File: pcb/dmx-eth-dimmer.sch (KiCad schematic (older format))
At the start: 38 parts, among them J1 MAINS IN, J2 STANDARD ENC28J60, J3 MINI ENC28J60, J4 MASTER PROG, SW1 IP1, SW2 IP2, SW3 IP3, SW4 IP4, SW5 DMXAH, SW6 DMXAL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

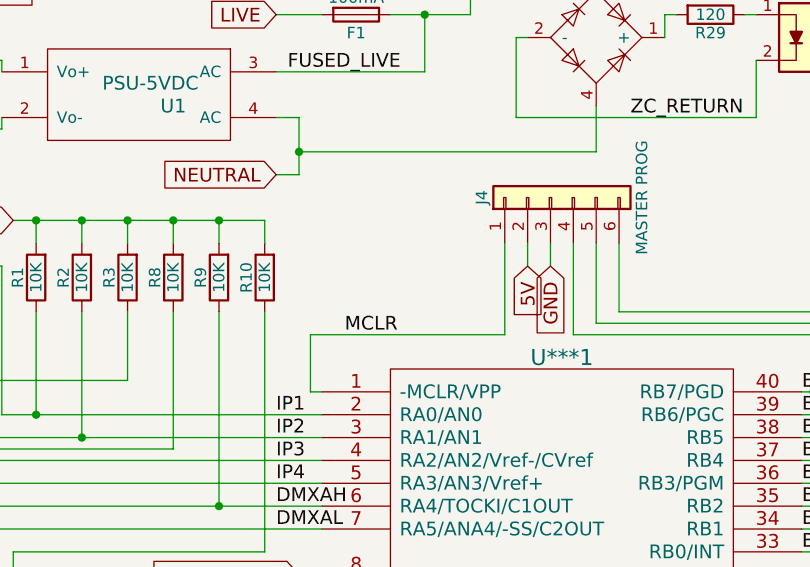
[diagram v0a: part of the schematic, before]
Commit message: PWM1/TMR1 version
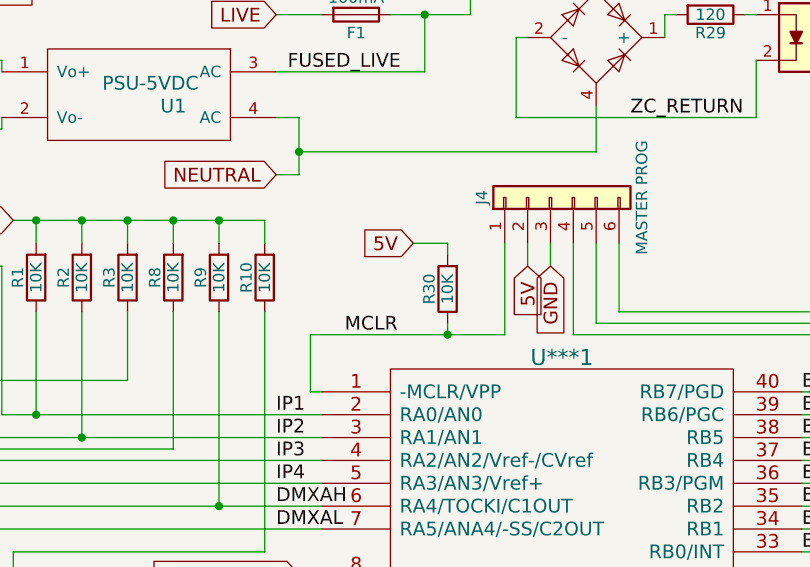
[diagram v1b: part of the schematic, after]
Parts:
- added R30: 10K, Resistors_THT:R_Axial_DIN0207_L6.3mm_D2.5mm_P10.16mm_Horizontal, symbol R
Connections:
- net 5V: now also R30.2
- net MCLR: now also R30.1
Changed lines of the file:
@@
 	1600 2050 1600 1950
 NoConn ~ 1500 1850
+$Comp
+L R R30
+U 1 1 5B40330D
+P 3750 2150
+F 0 "R30" V 3830 2150 50  0000 C CNN
+F 1 "10K" V 3750 2150 50  0000 C CNN
+F 2 "Resistors_THT:R_Axial_DIN0207_L6.3mm_D2.5mm_P10.16mm_Horizontal" V 3680 2150 50  0001 C CNN
+F 3 "" H 3750 2150 50  0001 C CNN
+	1    3750 2150
+	-1   0    0    1
+$EndComp
+Text GLabel 3600 1950 0    60   Input ~ 0
+5V
+Wire Wire Line
+	3600 1950 3750 1950
+Wire Wire Line
+	3750 1950 3750 2000
+Wire Wire Line
+	3750 2300 3750 2350
+Connection ~ 3750 2350
 $EndSCHEMATC

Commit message: New PCB Layout
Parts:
- removed J2: STANDARD ENC28J60, Pin_Headers:Pin_Header_Straight_2x06_Pitch2.54mm, symbol Conn_02x06_Counter_Clockwise
- removed J3: MINI ENC28J60, Pin_Headers:Pin_Header_Straight_2x05_Pitch2.54mm, symbol Conn_02x05_Counter_Clockwise
- removed U2: 3.3v Regulator, TO_SOT_Packages_THT:TO-220-3_Vertical, symbol L78L33_TO92
- added J3: STANDARD ENC28J60, Pin_Headers:Pin_Header_Straight_2x06_Pitch2.54mm, symbol Conn_02x06_Counter_Clockwise
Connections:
- net 5V: now also J3.11 (Pin_11)
- net CS: now also J3.4 (Pin_4)
- net DATACLK: now also J3.5 (Pin_5)
- net DMXAH: now also SW5.2
- net DMXAL: now also R10.1, SW6.4
- net GND: now also SW1.3, SW6.3, J3.12 (Pin_12), J3.2 (Pin_2)
- net INT: now also J3.9 (Pin_9)
- net IP1: now also SW1.2
- net IP2: now also SW2.2
- net IP3: now also R3.1, SW3.4
- net IP4: now also R8.1, SW4.4
- net RESET: now also J3.3 (Pin_3)
- net RX: now also J3.7 (Pin_7)
- net TX: now also J3.6 (Pin_6)
- no-connect marks 11 -> 4
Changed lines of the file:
@@
 Text GLabel 3000 3900 0    60   Input ~ 0
-GND
-$Comp
-L Conn_02x05_Counter_Clockwise J3
-U 1 1 5B1E6B11
-P 1550 6000
-F 0 "J3" H 1600 6300 50  0000 C CNN
-F 1 "MINI ENC28J60" H 1600 5700 50  0000 C CNN
-F 2 "Pin_Headers:Pin_Header_Straight_2x05_Pitch2.54mm" H 1550 6000 50  0001 C CNN
-F 3 "" H 1550 6000 50  0001 C CNN
-	1    1550 6000
-	1    0    0    -1
-$EndComp
-$Comp
-L Conn_02x06_Counter_Clockwise J2
-U 1 1 5B1E6B60
-P 1550 4900
-F 0 "J2" H 1600 5200 50  0000 C CNN
-F 1 "STANDARD ENC28J60" H 1600 4500 50  0000 C CNN
-F 2 "Pin_Headers:Pin_Header_Straight_2x06_Pitch2.54mm" H 1550 4900 50  0001 C CNN
-F 3 "" H 1550 4900 50  0001 C CNN
-	1    1550 4900
-	1    0    0    -1
-$EndComp
-$Comp
-L L78L33_TO92 U2
-U 1 1 5B1E721A
-P 2450 6200
-F 0 "U2" H 2300 6325 50  0000 C CNN
-F 1 "3.3v Regulator" H 2450 6325 50  0000 L CNN
-F 2 "TO_SOT_Packages_THT:TO-220-3_Vertical" H 2450 6425 50  0001 C CIN
-F 3 "" H 2450 6150 50  0001 C CNN
-	1    2450 6200
-	0    -1   -1   0
-$EndComp
-Text GLabel 1250 4700 0    60   Input ~ 0
-5V
-Text GLabel 2300 6550 0    60   Input ~ 0
-5V
-Text GLabel 1950 4700 2    60   Input ~ 0
-GND
-Text GLabel 2550 5800 2    60   Input ~ 0
-GND
-Text GLabel 2850 6200 2    60   Input ~ 0
 GND
 Text GLabel 3400 6700 0    60   Input ~ 0
@@
 Text Label 2650 5100 0    60   ~ 0
 CS
-Text Label 2650 5450 0    60   ~ 0
+Text Label 2750 6350 0    60   ~ 0
 RX
-Text Label 2650 5550 0    60   ~ 0
+Text Label 2750 6150 0    60   ~ 0
 INT
-NoConn ~ 1850 4800
-NoConn ~ 1350 5200
 Text GLabel 6150 2500 1    60   Input ~ 0
 GND
@@
 F 3 "" H 1250 2350 50  0001 C CNN
 	1    1250 2150
-	1    0    0    -1
-$EndComp
-$Comp
-L SW_Push_4PIN SW3
-U 1 1 5B1EF7C8
-P 1250 2450
-F 0 "SW3" H 1300 2550 50  0000 L CNN
-F 1 "IP3" H 1250 2390 50  0000 C CNN
-F 2 "CarnivalBen:SW_PUSH_6mm_4pin" H 1250 2650 50  0001 C CNN
-F 3 "" H 1250 2650 50  0001 C CNN
-	1    1250 2450
 	1    0    0    -1
 $EndComp
@@
 	0    1    1    0
 $EndComp
-Text GLabel 1250 4800 0    60   Input ~ 0
-GND
-NoConn ~ 1350 5000
-NoConn ~ 1350 5800
-NoConn ~ 1350 6000
 $Comp
 L 74HCT08 U3
@@
 Entry Wire Line
 	5600 4550 5700 4650
-NoConn ~ 1500 3050
-NoConn ~ 1500 2150
-NoConn ~ 1000 1950
 Wire Wire Line
 	1800 1150 1800 1200
@@
 	2200 4250 3200 4250
 Wire Wire Line
-	2750 6200 2850 6200
-Wire Wire Line
-	1850 4700 1950 4700
-Wire Wire Line
-	1350 4700 1250 4700
-Wire Wire Line
 	3200 4700 2400 4700
 Wire Wire Line
 	2400 4700 2400 5400
 Wire Wire Line
-	900  5450 3250 5450
-Wire Wire Line
 	3200 4900 2500 4900
 Wire Wire Line
 	2500 4900 2500 5500
 Wire Wire Line
-	2500 5500 950  5500
-Wire Wire Line
-	850  5550 3300 5550
-Wire Wire Line
 	2550 5100 3200 5100
 Wire Wire Line
 	3200 4600 2350 4600
 Wire Wire Line
-	2350 4600 2350 5350
-Wire Wire Line
 	3500 6100 3450 6100
 Wire Wire Line
@@
 	3150 5350 3350 5350
 Wire Wire Line
-	3300 5550 3300 6150
-Wire Wire Line
-	3250 5450 3250 6450
-Wire Wire Line
-	3250 6450 3450 6450
+	3050 6450 3450 6450
 Connection ~ 3450 6450
-Wire Wire Line
-	3300 6150 3450 6150
 Wire Wire Line
 	3450 6100 3450 6200
@@
 	4700 950  4700 1050
 Wire Wire Line
-	1250 4800 1350 4800
-Wire Wire Line
-	850  4900 850  5900
-Wire Wire Line
-	850  4900 1350 4900
-Wire Wire Line
-	900  5100 900  6100
-Wire Wire Line
-	900  5100 1350 5100
-Wire Wire Line
-	2000 5500 2000 5100
-Wire Wire Line
-	2000 5100 1850 5100
-Wire Wire Line
-	1850 5200 2050 5200
-Wire Wire Line
-	2050 5200 2050 6200
-Connection ~ 2050 5400
-Wire Wire Line
-	1850 5000 2100 5000
-Wire Wire Line
-	2100 5000 2100 6000
-Connection ~ 2100 5350
-Wire Wire Line
 	2550 5100 2550 5600
-Wire Wire Line
-	2550 5600 2150 5600
-Wire Wire Line
-	2150 4900 2150 6100
-Wire Wire Line
-	2150 4900 1850 4900
-Wire Wire Line
-	1850 5800 2550 5800
-Wire Wire Line
-	850  5900 1350 5900
-Connection ~ 850  5550
-Wire Wire Line
-	900  6100 1350 6100
-Connection ~ 900  5450
-Wire Wire Line
-	1350 6200 950  6200
-Wire Wire Line
-	950  6200 950  5500
-Connection ~ 2000 5500
-Wire Wire Line
-	2050 6200 1850 6200
-Wire Wire Line
-	2400 5400 2050 5400
-Wire Wire Line
-	2150 6100 1850 6100
-Connection ~ 2150 5600
-Wire Wire Line
-	2100 6000 1850 6000
-Wire Wire Line
-	2350 5350 2100 5350
-Wire Wire Line
-	2450 6500 2450 6550
-Wire Wire Line
-	2450 6550 2300 6550
-Wire Wire Line
-	1850 5900 2450 5900
 Wire Wire Line
 	5000 6700 5100 6700
@@
 	1800 2050 1600 2050
 Wire Wire Line
-	1550 2200 1550 2250
+	1550 2150 1550 2250
 Wire Wire Line
 	1650 2900 1650 2450
@@
 	1650 2450 1500 2450
 Wire Wire Line
-	2350 2250 2350 2550
-Wire Wire Line
-	2350 2550 1500 2550
-Wire Wire Line
 	1600 3000 1600 2750
 Wire Wire Line
 	1600 2750 1500 2750
 Wire Wire Line
-	2550 2250 2550 2850
-Wire Wire Line
-	2550 2850 1500 2850
-Wire Wire Line
-	1550 3100 1550 3150
-Wire Wire Line
-	1750 3200 1750 3350
+	1550 3050 1550 3150
+Wire Wire Line
+	1750 3200 1750 3450
 Wire Wire Line
 	1750 3350 1500 3350
 Wire Wire Line
-	2950 2250 2950 3300
-Wire Wire Line
-	2950 3300 1850 3300
-Wire Wire Line
-	1850 3300 1850 3450
-Wire Wire Line
-	1850 3450 1500 3450
-Wire Wire Line
-	900  1850 900  3350
-NoConn ~ 1000 3450
-Wire Wire Line
-	1600 2050 1600 1950
-NoConn ~ 1500 1850
+	900  1850 900  3450
+Wire Wire Line
+	1600 2050 1600 1850
 $Comp
 L R R30
@@
 	3750 2300 3750 2350
 Connection ~ 3750 2350
+Wire Wire Line
+	1000 1950 900  1950
+Connection ~ 900  1950
+Wire Wire Line
+	900  3450 1000 3450
+Connection ~ 900  3350
+Wire Wire Line
+	1500 3050 1550 3050
+Connection ~ 1550 3100
+Wire Wire Line
+	1500 2150 1550 2150
+Connection ~ 1550 2200
+Wire Wire Line
+	1600 1850 1500 1850
+Connection ~ 1600 1950
+$Comp
+L SW_Push_4PIN SW3
+U 1 1 5B1EF7C8
+P 1250 2450
+F 0 "SW3" H 1300 2550 50  0000 L CNN
+F 1 "IP3" H 1250 2390 50  0000 C CNN
+F 2 "CarnivalBen:SW_PUSH_6mm_4pin" H 1250 2650 50  0001 C CNN
+F 3 "" H 1250 2650 50  0001 C CNN
+	1    1250 2450
+	1    0    0    -1
+$EndComp
+Wire Wire Line
+	1500 2550 1650 2550
+Connection ~ 1650 2550
+Wire Wire Line
+	2350 2250 2350 2900
+Connection ~ 2350 2900
+Wire Wire Line
+	1500 2850 1600 2850
+Connection ~ 1600 2850
+Wire Wire Line
+	2550 2250 2550 3000
+Connection ~ 2550 3000
+Wire Wire Line
+	1750 3450 1500 3450
+Connection ~ 1750 3350
+Wire Wire Line
+	2950 2250 2950 3200
+Connection ~ 2950 3200
+$Comp
+L Conn_02x06_Counter_Clockwise J3
+U 1 1 5B643410
+P 2050 6050
+F 0 "J3" H 2100 6350 50  0000 C CNN
+F 1 "STANDARD ENC28J60" H 2100 5650 50  0000 C CNN
+F 2 "Pin_Headers:Pin_Header_Straight_2x06_Pitch2.54mm" H 2050 6050 50  0001 C CNN
+F 3 "" H 2050 6050 50  0001 C CNN
+	1    2050 6050
+	1    0    0    -1
+$EndComp
+Text GLabel 2450 5950 2    60   Input ~ 0
+5V
+Text GLabel 1750 5950 0    60   Input ~ 0
+GND
+Text GLabel 2450 5850 2    60   Input ~ 0
+GND
+NoConn ~ 1850 5850
+NoConn ~ 2350 6250
+Wire Wire Line
+	2550 5600 1400 5600
+Wire Wire Line
+	1400 5600 1400 6150
+Wire Wire Line
+	1400 6150 1850 6150
+Wire Wire Line
+	1850 5950 1750 5950
+Wire Wire Line
+	2350 5950 2450 5950
+Wire Wire Line
+	2450 5850 2350 5850
+Wire Wire Line
+	2500 5500 1350 5500
+Wire Wire Line
+	1350 5500 1350 6350
+Wire Wire Line
+	1350 6350 1850 6350
+Wire Wire Line
+	2400 5400 1300 5400
+Wire Wire Line
+	1300 5400 1300 6250
+Wire Wire Line
+	1300 6250 1850 6250
+Wire Wire Line
+	2350 4600 2350 5650
+Wire Wire Line
+	2350 5650 1250 5650
+Wire Wire Line
+	1250 5650 1250 6050
+Wire Wire Line
+	1250 6050 1850 6050
+Wire Wire Line
+	3050 6450 3050 6350
+Wire Wire Line
+	3050 6350 2350 6350
+Wire Wire Line
+	3450 6150 2350 6150
+NoConn ~ 2350 6050
 $EndSCHEMATC
